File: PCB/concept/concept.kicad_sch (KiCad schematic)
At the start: 43 parts, among them J1 Antenna, J4 SSD1306 I2C Display, SW1 RotaryEncoder_Switch, U2 Pico

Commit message: Fix error in schematic
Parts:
- C? (x2): value 27p -> 220p
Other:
- note added: "R9, R10, C17, C18 op-amp cutoff 1/(2 * pi * 220e-12 * 56e3) ~= 12kHz"
- note removed: "R9, R10, C17, C18 op-amp cutoff 1/(2 * pi * 82e-12 * 100e3) ~= 12kHz"
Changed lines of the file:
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@@
     (effects (font (size 2 2)) (justify left bottom))
   )
-  (text "R9, R10, C17, C18  op-amp cutoff\n1/(2 * pi * 82e-12 * 100e3) ~= 12kHz"
+  (text "R9, R10, C17, C18  op-amp cutoff\n1/(2 * pi * 220e-12 * 56e3) ~= 12kHz"
     (at 70.485 111.125 0)
     (effects (font (size 2 2)) (justify left bottom))
@@
       (effects (font (size 1.27 1.27)))
     )
-    (property "Value" "27p" (at 193.675 57.531 90)
+    (property "Value" "220p" (at 193.675 57.531 90)
       (effects (font (size 1.27 1.27)))
     )
@@
       (effects (font (size 1.27 1.27)))
     )
-    (property "Value" "27p" (at 193.675 15.621 90)
-      (effects (font (size 1.27 1.27)))
-    )
+    (property "Value" "220p" (at 193.675 15.621 90)
+      (effects (font (size 1.27 1.27)))
+    )

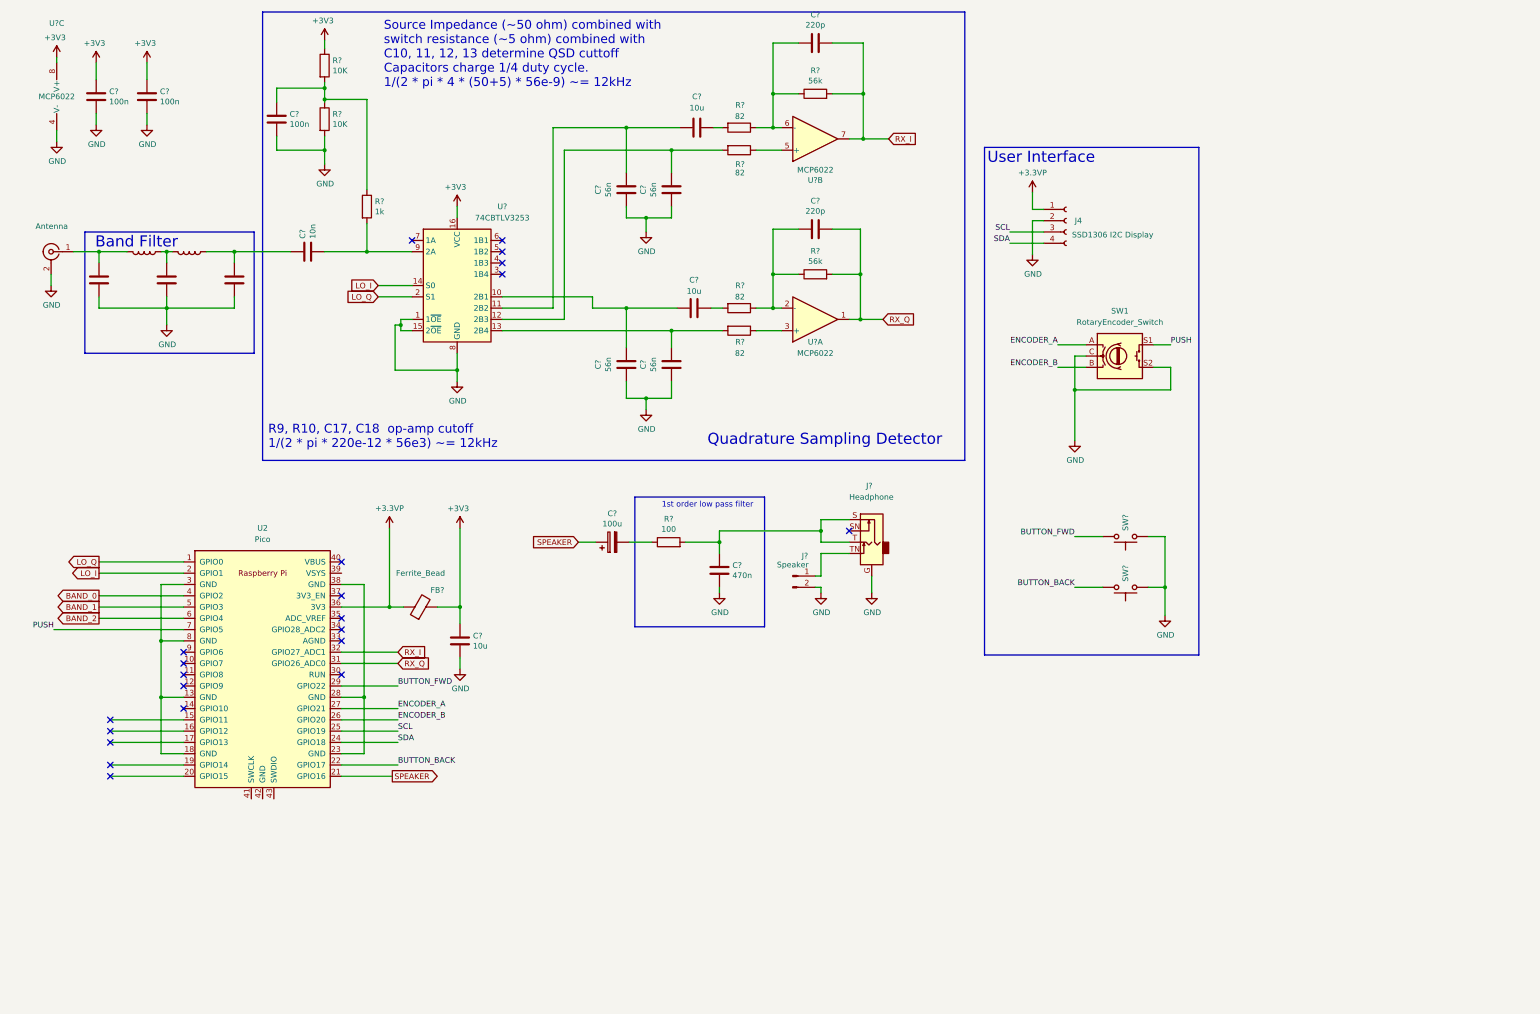
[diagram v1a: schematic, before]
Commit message: Add noise reduction animation and update concept schematic
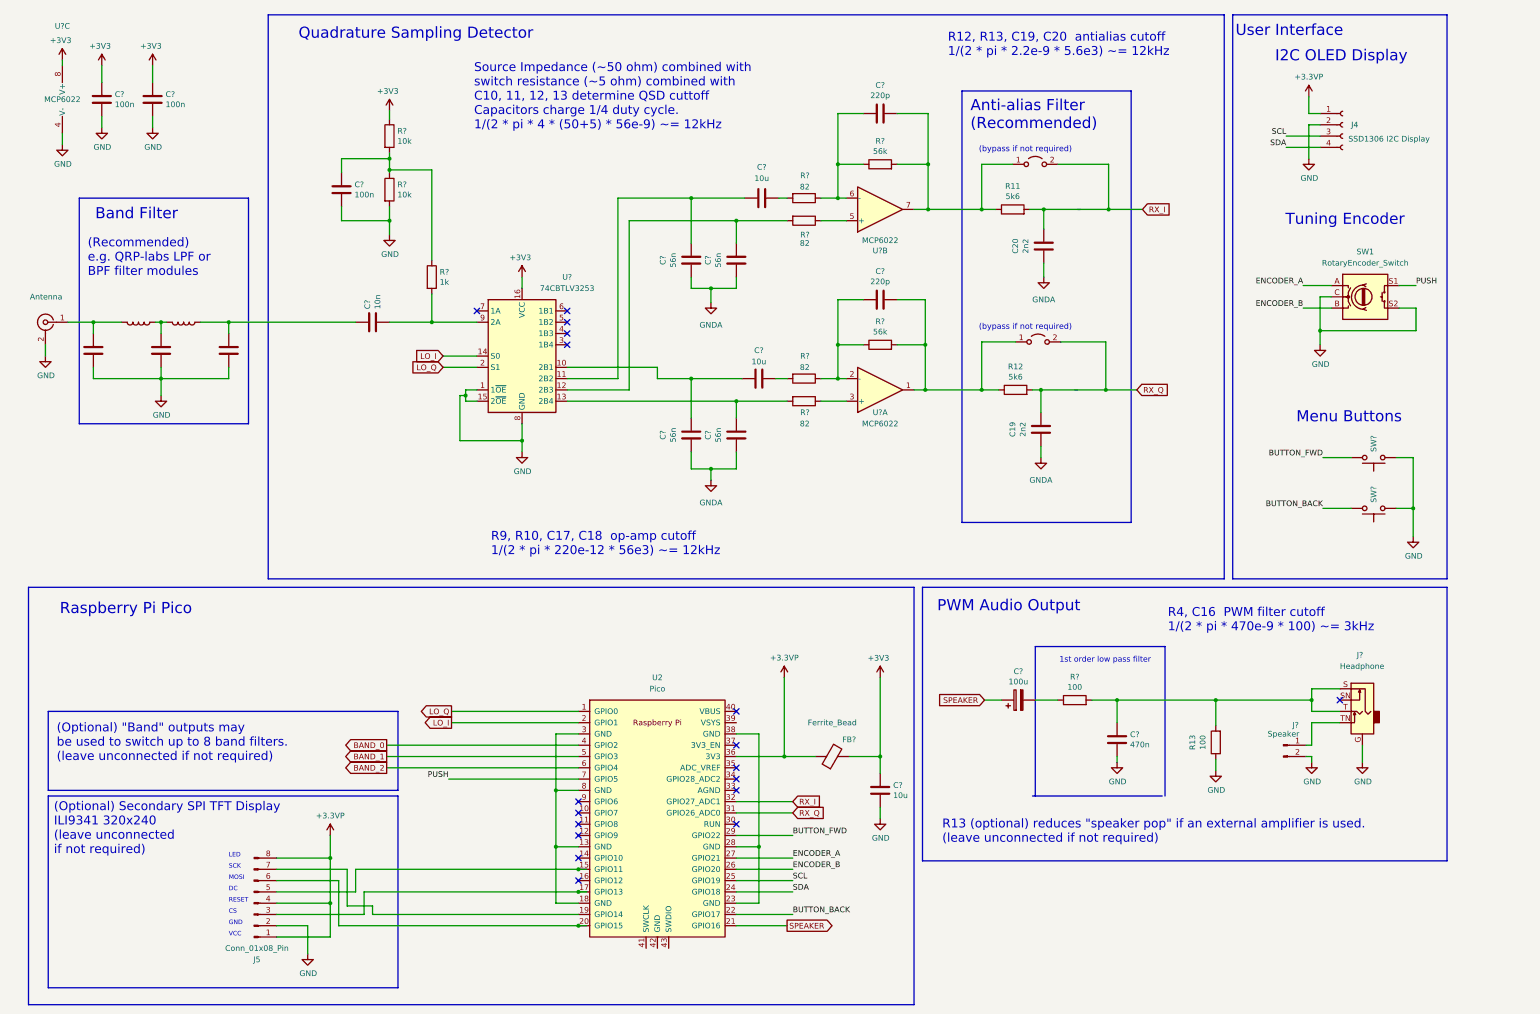
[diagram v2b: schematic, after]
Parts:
- added C19, C20: 2n2, Capacitor_SMD:C_0805_2012Metric, symbol Device:C
- added J5: Conn_01x08_Pin, symbol Connector:Conn_01x08_Pin
- added JP1, JP2: Jumper_2_Open, symbol Jumper:Jumper_2_Open
- added R11, R12: 5k6, Resistor_SMD:R_0805_2012Metric, symbol Device:R
- added R13: 100, Resistor_SMD:R_0805_2012Metric, symbol Device:R
- R? (x2): value 10K -> 10k
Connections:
- net +3.3VP: now also J5.1 (Pin_1), J5.4 (Pin_4), J5.8 (Pin_8)
- net GND: now also J5.2 (Pin_2), R13.1; no longer C?.1, C?.1, C?.1, C?.1
- net RX_I: now also C20.2, JP1.2 (B), R11.2; no longer C?.2, R?.2, U?.7
- net RX_Q: now also C19.2, JP2.2 (B), R12.2; no longer C?.2, R?.2, U?.1
- net at U2.15 (GPIO11): now also J5.5 (Pin_5)
- net at U2.17 (GPIO13): now also J5.3 (Pin_3)
- net at U2.19 (GPIO14): now also J5.7 (Pin_7)
- net at U2.20 (GPIO15): now also J5.6 (Pin_6)
- net at C?.1, J?.S, J?.T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: now also R13.2
- new net: C?.2, JP2.1 (A), R12.1, R?.2, U?.1
- new net: C?.2, JP1.1 (A), R11.1, R?.2, U?.7
- new net GNDA: C19.1, C20.1, C?.1, C?.1, C?.1, C?.1
- no-connect marks 22 -> 18
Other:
- note added: "(Optional) "Band" outputs may be used to switch up to 8 band filters. (leave unconnected if not required)"
- note added: "(Optional) Secondary SPI TFT Display ILI9341 320x240 (leave unconnected if not required)"
- note added: "(Recommended) e.g. QRP-labs LPF or BPF filter modules"
- note added: "(bypass if not required)"
- note added: "Anti-alias Filter (Recommended)"
- note added: "CS"
- note added: "DC"
- note added: "GND"
- note added: "I2C OLED Display"
- note added: "LED"
- note added: "MOSI"
- note added: "Menu Buttons"
- note added: "PWM Audio Output"
- note added: "R12, R13, C19, C20 antialias cutoff 1/(2 * pi * 2.2e-9 * 5.6e3) ~= 12kHz"
- note added: "R13 (optional) reduces "speaker pop" if an external amplifier is used. (leave unconnected if not required)"
- note added: "R4, C16 PWM filter cutoff 1/(2 * pi * 470e-9 * 100) ~= 3kHz"
- note added: "RESET"
- note added: "Raspberry Pi Pico"
- note added: "SCK"
- note added: "Tuning Encoder"
- note added: "VCC"
- moved on the sheet: C?, FB?, J4, J?, R?, SW1, SW?, U2, U?, U?A, U?B, U?C
